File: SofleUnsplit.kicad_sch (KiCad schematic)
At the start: 118 parts, among them J1 Conn_01x05, SW1 Switch, SW10 Switch, SW11 Switch, SW12 Switch, SW13 Switch, SW14 Switch, SW15 Switch, SW16 Switch, SW17 Switch, SW18 Switch, SW19 Switch, SW2 Switch, SW20 Switch, SW21 Switch, SW22 Switch, SW23 Switch, SW24 Switch, SW25 Switch, SW26 Switch, SW27 Switch, SW28 Switch, SW29 Switch, SW3 Switch, SW30 Switch, SW31 Switch, SW32 Switch, SW33 Switch, SW34 Switch, SW35 Switch, SW36 Switch, SW37 Switch, SW38 Switch, SW39 Switch, SW4 Switch, SW40 Switch, SW41 Switch, SW42 Switch, SW43 Switch, SW44 Switch, SW45 Switch, SW46 Switch, SW47 Switch, SW48 Switch, SW49 Switch, SW5 Switch, SW50 Switch, SW51 Switch, SW52 Switch, SW53 Switch, SW54 Switch, SW55 Switch, SW56 Switch, SW57 Switch, SW58 Switch, SW6 Switch, SW7 Switch, SW8 Switch, SW9 Switch, U1 MCU_rp2040-zero

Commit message: First version, final, before last check.
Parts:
- added G1: ~, local:josef_adamcik_20mm_cu_mask, symbol symbols:logo_josef
- added H1, H2, H3, H4: MountingHole, MountingHole:MountingHole_2.7mm_M2.5_DIN965, symbol Mechanical:MountingHole
- added H5, H6, H7, H8: MountingHole, MountingHole:MountingHole_3.2mm_M3_DIN965, symbol Mechanical:MountingHole
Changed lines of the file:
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@@
+    )
+  )
+  (symbol (lib_id "Mechanical:MountingHole") (at 387.35 29.21 0) (unit 1)
+    (in_bom yes) (on_board yes) (dnp no) (fields_autoplaced)
+    (property "Reference" "H2" (at 389.89 28.575 0)
+      (effects (font (size 1.27 1.27)) (justify left))
+    )
+    (property "Value" "MountingHole" (at 389.89 31.115 0)
+      (effects (font (size 1.27 1.27)) (justify left))
+    )
+    (property "Footprint" "MountingHole:MountingHole_2.7mm_M2.5_DIN965" (at 387.35 29.21 0)
+      (effects (font (size 1.27 1.27)) hide)
+    )
+    (property "Datasheet" "~" (at 387.35 29.21 0)
+      (effects (font (size 1.27 1.27)) hide)
+    )
+    (instances
+      (project "SofleUnsplit"
+        (path "/0271784e-2195-481b-b0c9-914478a67f87"
+          (reference "H2") (unit 1)
+        )
+      )
+    )
+  )
+  (symbol (lib_id "Mechanical:MountingHole") (at 387.35 36.83 0) (unit 1)
+    (in_bom yes) (on_board yes) (dnp no) (fields_autoplaced)
+    (property "Reference" "H3" (at 389.89 36.195 0)
+      (effects (font (size 1.27 1.27)) (justify left))
+    )
+    (property "Value" "MountingHole" (at 389.89 38.735 0)
+      (effects (font (size 1.27 1.27)) (justify left))
+    )
+    (property "Footprint" "MountingHole:MountingHole_2.7mm_M2.5_DIN965" (at 387.35 36.83 0)
+      (effects (font (size 1.27 1.27)) hide)
+    )
+    (property "Datasheet" "~" (at 387.35 36.83 0)
+      (effects (font (size 1.27 1.27)) hide)
+    )
+    (instances
+      (project "SofleUnsplit"
+        (path "/0271784e-2195-481b-b0c9-914478a67f87"
+          (reference "H3") (unit 1)
+        )
+      )
     )
   )
@@
     )
   )
+  (symbol (lib_id "Mechanical:MountingHole") (at 387.35 62.23 0) (unit 1)
+    (in_bom yes) (on_board yes) (dnp no) (fields_autoplaced)
+    (property "Reference" "H7" (at 389.89 61.595 0)
+      (effects (font (size 1.27 1.27)) (justify left))
+    )
+    (property "Value" "MountingHole" (at 389.89 64.135 0)
+      (effects (font (size 1.27 1.27)) (justify left))
+    )
+    (property "Footprint" "MountingHole:MountingHole_3.2mm_M3_DIN965" (at 387.35 62.23 0)
+      (effects (font (size 1.27 1.27)) hide)
+    )
+    (property "Datasheet" "~" (at 387.35 62.23 0)
+      (effects (font (size 1.27 1.27)) hide)
+    )
+    (instances
+      (project "SofleUnsplit"
+        (path "/0271784e-2195-481b-b0c9-914478a67f87"
+          (reference "H7") (unit 1)
+        )
+      )
+    )
+  )
   (symbol (lib_id "zzkeeb:Switch") (at 144.78 217.17 0) (unit 1)
     (in_bom yes) (on_board yes) (dnp no)
@@
     )
   )
+  (symbol (lib_id "Mechanical:MountingHole") (at 387.35 68.58 0) (unit 1)
+    (in_bom yes) (on_board yes) (dnp no) (fields_autoplaced)
+    (property "Reference" "H8" (at 389.89 67.945 0)
+      (effects (font (size 1.27 1.27)) (justify left))
+    )
+    (property "Value" "MountingHole" (at 389.89 70.485 0)
+      (effects (font (size 1.27 1.27)) (justify left))
+    )
+    (property "Footprint" "MountingHole:MountingHole_3.2mm_M3_DIN965" (at 387.35 68.58 0)
+      (effects (font (size 1.27 1.27)) hide)
+    )
+    (property "Datasheet" "~" (at 387.35 68.58 0)
+      (effects (font (size 1.27 1.27)) hide)
+    )
+    (instances
+      (project "SofleUnsplit"
+        (path "/0271784e-2195-481b-b0c9-914478a67f87"
+          (reference "H8") (unit 1)
+        )
+      )
+    )
+  )
   (symbol (lib_id "zzkeeb:Switch") (at 59.69 217.17 0) (unit 1)
     (in_bom yes) (on_board yes) (dnp no)
@@
         (path "/0271784e-2195-481b-b0c9-914478a67f87"
           (reference "SW15") (unit 1)
+        )
+      )
+    )
+  )
+  (symbol (lib_id "Mechanical:MountingHole") (at 387.35 55.88 0) (unit 1)
+    (in_bom yes) (on_board yes) (dnp no) (fields_autoplaced)
+    (property "Reference" "H6" (at 389.89 55.245 0)
+      (effects (font (size 1.27 1.27)) (justify left))
+    )
+    (property "Value" "MountingHole" (at 389.89 57.785 0)
+      (effects (font (size 1.27 1.27)) (justify left))
+    )
+    (property "Footprint" "MountingHole:MountingHole_3.2mm_M3_DIN965" (at 387.35 55.88 0)
+      (effects (font (size 1.27 1.27)) hide)
+    )
+    (property "Datasheet" "~" (at 387.35 55.88 0)
+      (effects (font (size 1.27 1.27)) hide)
+    )
+    (instances
+      (project "SofleUnsplit"
+        (path "/0271784e-2195-481b-b0c9-914478a67f87"
+          (reference "H6") (unit 1)
         )
       )
@@
         (path "/0271784e-2195-481b-b0c9-914478a67f87"
           (reference "D19") (unit 1)
+        )
+      )
+    )
+  )
+  (symbol (lib_id "Mechanical:MountingHole") (at 387.35 49.53 0) (unit 1)
+    (in_bom yes) (on_board yes) (dnp no) (fields_autoplaced)
+    (property "Reference" "H5" (at 389.89 48.895 0)
+      (effects (font (size 1.27 1.27)) (justify left))
+    )
+    (property "Value" "MountingHole" (at 389.89 51.435 0)
+      (effects (font (size 1.27 1.27)) (justify left))
+    )
+    (property "Footprint" "MountingHole:MountingHole_3.2mm_M3_DIN965" (at 387.35 49.53 0)
+      (effects (font (size 1.27 1.27)) hide)
+    )
+    (property "Datasheet" "~" (at 387.35 49.53 0)
+      (effects (font (size 1.27 1.27)) hide)
+    )
+    (instances
+      (project "SofleUnsplit"
+        (path "/0271784e-2195-481b-b0c9-914478a67f87"
+          (reference "H5") (unit 1)
         )
       )
@@
     )
   )
+  (symbol (lib_id "symbols:logo_josef") (at 388.62 80.01 0) (unit 1)
+    (in_bom no) (on_board yes) (dnp no) (fields_autoplaced)
+    (property "Reference" "G1" (at 392.43 80.645 0)
+      (effects (font (size 1.27 1.27)) (justify left))
+    )
+    (property "Value" "~" (at 388.62 80.01 0)
+      (effects (font (size 1.27 1.27)))
+    )
+    (property "Footprint" "local:josef_adamcik_20mm_cu_mask" (at 388.62 80.01 0)
+      (effects (font (size 1.27 1.27)) hide)
+    )
+    (property "Datasheet" "" (at 388.62 80.01 0)
+      (effects (font (size 1.27 1.27)) hide)
+    )
+    (instances
+      (project "SofleUnsplit"
+        (path "/0271784e-2195-481b-b0c9-914478a67f87"
+          (reference "G1") (unit 1)
+        )
+      )
+    )
+  )
   (symbol (lib_id "zzkeeb:Switch") (at 144.78 200.66 0) (unit 1)
     (in_bom yes) (on_board yes) (dnp no)
@@
         )
       )
+    )
+  )
+  (symbol (lib_id "Mechanical:MountingHole") (at 387.35 21.59 0) (unit 1)
+    (in_bom yes) (on_board yes) (dnp no) (fields_autoplaced)
+    (property "Reference" "H1" (at 389.89 20.955 0)
+      (effects (font (size 1.27 1.27)) (justify left))
+    )
+    (property "Value" "MountingHole" (at 389.89 23.495 0)
+      (effects (font (size 1.27 1.27)) (justify left))
+    )
+    (property "Footprint" "MountingHole:MountingHole_2.7mm_M2.5_DIN965" (at 387.35 21.59 0)
+      (effects (font (size 1.27 1.27)) hide)
+    )
+    (property "Datasheet" "~" (at 387.35 21.59 0)
+      (effects (font (size 1.27 1.27)) hide)
+    )
+    (instances
+      (project "SofleUnsplit"
+        (path "/0271784e-2195-481b-b0c9-914478a67f87"
+          (reference "H1") (unit 1)
+        )
+      )
+    )
+  )
+  (symbol (lib_id "Mechanical:MountingHole") (at 387.35 43.18 0) (unit 1)
+    (in_bom yes) (on_board yes) (dnp no) (fields_autoplaced)
+    (property "Reference" "H4" (at 389.89 42.545 0)
+      (effects (font (size 1.27 1.27)) (justify left))
+    )
+    (property "Value" "MountingHole" (at 389.89 45.085 0)
+      (effects (font (size 1.27 1.27)) (justify left))
+    )
+    (property "Footprint" "MountingHole:MountingHole_2.7mm_M2.5_DIN965" (at 387.35 43.18 0)
+      (effects (font (size 1.27 1.27)) hide)
+    )
+    (property "Datasheet" "~" (at 387.35 43.18 0)
+      (effects (font (size 1.27 1.27)) hide)
+    )
+    (instances
+      (project "SofleUnsplit"
+        (path "/0271784e-2195-481b-b0c9-914478a67f87"
+          (reference "H4") (unit 1)
+        )
+      )

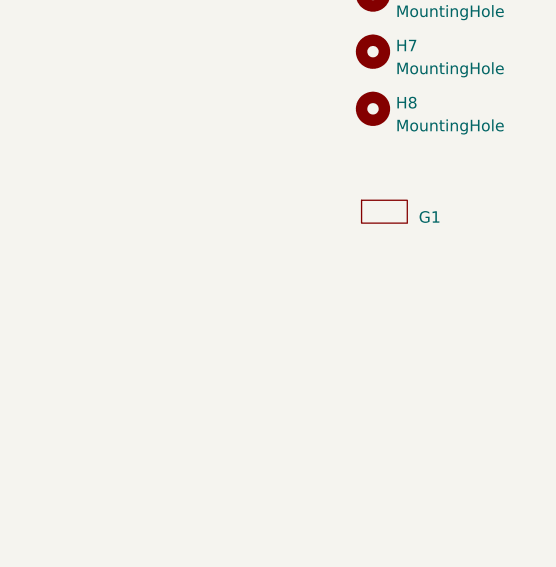
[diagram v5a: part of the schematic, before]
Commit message: Ues SOD-123 layout for dioedes (might be easier to solder by hand than SOD-123F even though I have SOD-123F diodes). Logo as footprint in copper.
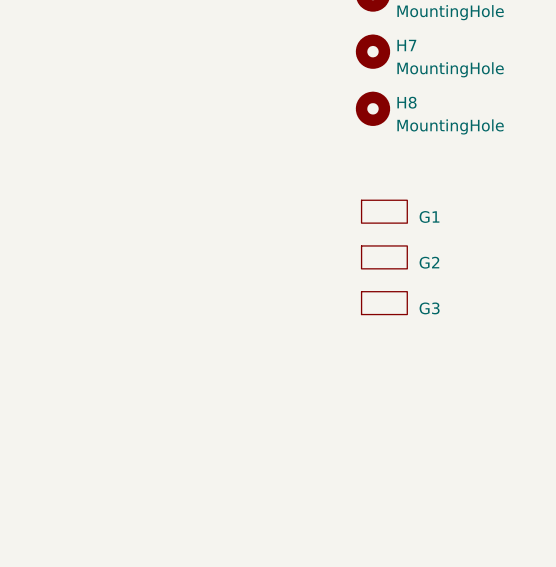
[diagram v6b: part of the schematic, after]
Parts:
- added G2, G3: ~, local:logo_stanya_cu_mask, symbol symbols:logo_stanya
- D1, D10, D11, D12, D13, D14, D15, D16, D17, D18, D19, D2, D20, D21, D22, D23, D24, D25, D26, D27, D28, D29, D3, D30, D31, D32, D33, D34, D35, D36, D37, D38, D39, D4, D40, D41, D42, D43, D44, D45, D46, D47, D48, D49, D5, D50, D51, D52, D53, D54, D55, D56, D57, D58, D6, D7, D8, D9: footprint Diode_SMD:D_SOD-123F -> Diode_SMD:D_SOD-123
